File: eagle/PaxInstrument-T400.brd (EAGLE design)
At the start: 99.1 x 53.3 mm, 137 parts, among them IC1 MCP3424, IC3 SN74LVC1G74DCT, J1 MICRO-SDCARD-CONNECTOR-330006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, Q1 DMP2035U-7, Q2 DMP2035U-7, Q3 DMN2075U-7, Q4 DMN2075U-7, Q5 DMP2035U-7, U1 MCP9800, U2 APX809, U3 MCP73831, U4 MIC5219-3.3V, X1 FH12-12S-1S, Y1 RESONATORSMD

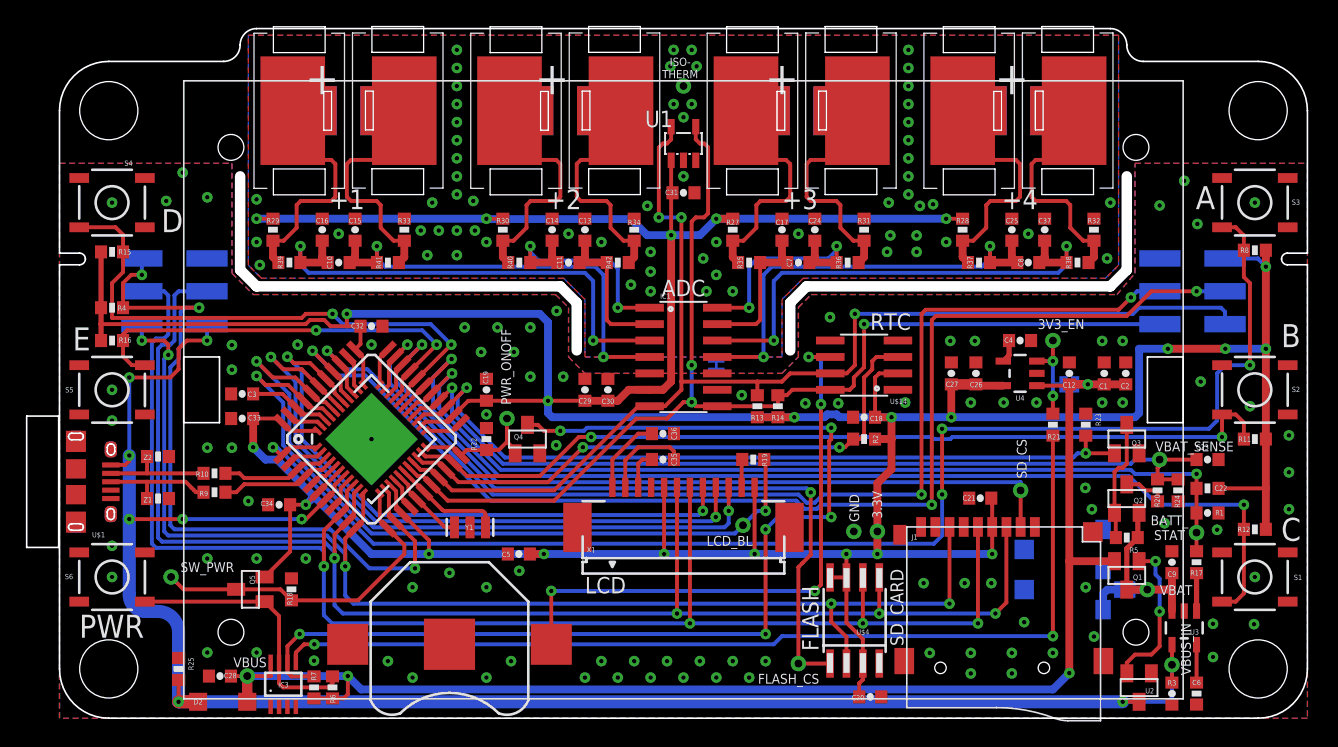
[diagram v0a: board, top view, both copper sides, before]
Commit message: Remove a lot and replace atmega with stm32f103
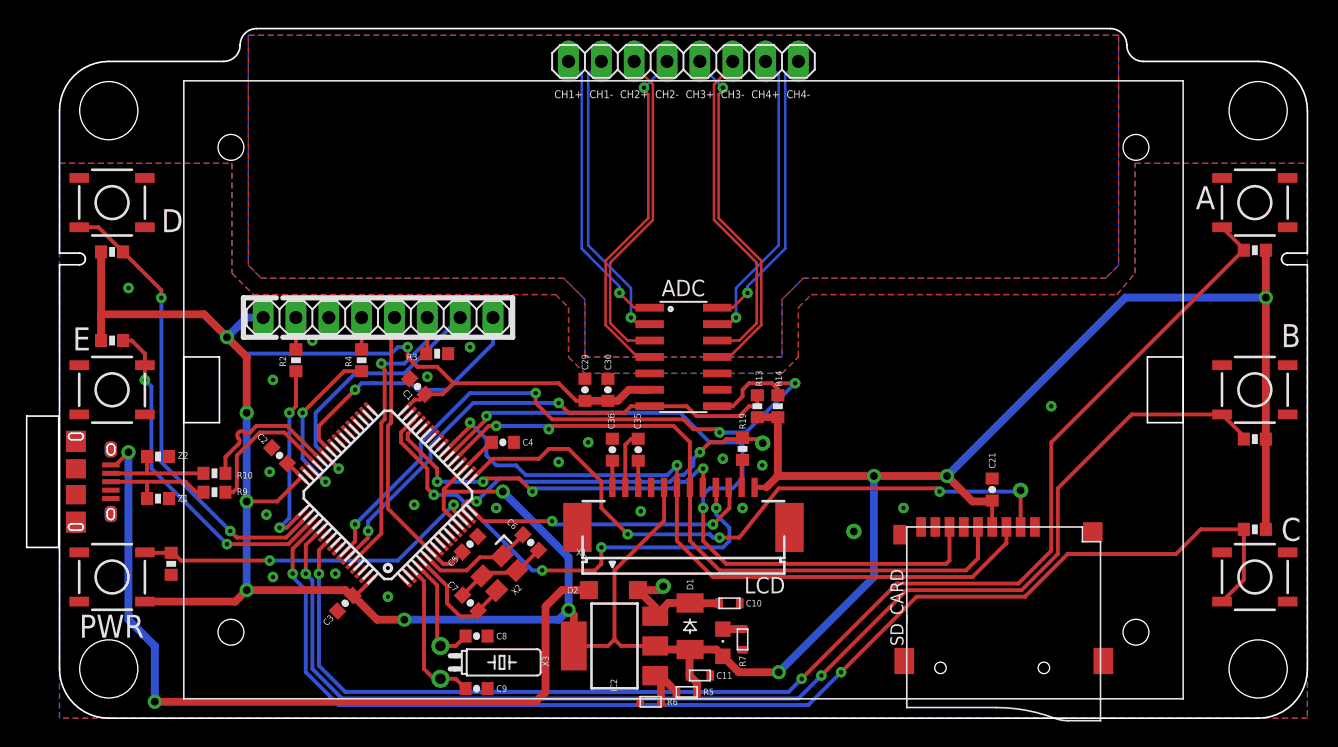
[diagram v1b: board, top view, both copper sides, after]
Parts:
- removed BAT1: (no value), SparkFun-Electromechanical:BATTCON_12MM
- removed C12, C22, C26: 10uF, PaxInstrument-T400:SPARKFUN-CAPACITORS_0603-CAP
- removed C13, C14, C15, C16, C17, C18, C20, C24, C25, C27, C28, C31, C32, C33, C34, C37: 0.1uF, PaxInstrument-T400:SPARKFUN-CAPACITORS_0603-CAP
- removed C19, C23: 1uF, PaxInstrument-T400:SPARKFUN-CAPACITORS_0603-CAP
- removed GND: SPARKFUN-DIGITALIC_QFN_ATMEGA32U4, PaxInstrument-T400:SPARKFUN-DIGITALIC_SPARKFUN-DIGITALIC_QFN-44
- removed IC3: SN74LVC1G74DCT, PaxInstrument-T400:SSOP8
- removed ICSP, ICSP1: ICSP, PaxInstrument-T400:SPARKFUN-CONNECTORS_2X3_SMT_POSTS_PAXINSTRUMENT
- removed JP1: ON, SparkFun-Passives:SJ_2S-NO
- removed Q1, Q2, Q5: DMP2035U-7, PaxInstrument-T400:SOT23
- removed Q3, Q4: DMN2075U-7, PaxInstrument-T400:SOT23
- removed R17: 2k, PaxInstrument-T400:SPARKFUN-RESISTORS_0603-RES
- removed R18, R21, R22, R23: 10k, PaxInstrument-T400:SPARKFUN-RESISTORS_0603-RES
- removed R20: 18.7K, PaxInstrument-T400:SPARKFUN-RESISTORS_0603-RES
- removed R24: 34K, PaxInstrument-T400:SPARKFUN-RESISTORS_0603-RES
- removed R25: 4.7k, PaxInstrument-T400:SPARKFUN-RESISTORS_0603-RES
- removed R27, R28, R29, R30, R31, R32, R33, R34: 1M, PaxInstrument-T400:SPARKFUN-RESISTORS_0603-RES
- removed R35, R36, R37, R38, R39, R40, R41, R42: 499R, PaxInstrument-T400:SPARKFUN-RESISTORS_0603-RES
- removed SJ1, SJ2: JUMPER-PAD-2-NC_BY_TRACE, SparkFun-Passives:PAD-JUMPER-2-NC_BY_TRACE_YES_SILK
- removed TP1: PWR_ONOFF, PaxInstrument-T400:TP_15TH
- removed TP11: VBUS_IN, PaxInstrument-T400:TP_15TH
- removed TP13: 3.3V, PaxInstrument-T400:TP_15TH
- removed TP14: VBAT, PaxInstrument-T400:TP_15TH
- removed TP2: 3V3_EN, PaxInstrument-T400:TP_15TH
- removed TP3: BATT_STAT, PaxInstrument-T400:TP_15TH
- removed TP4: VBAT_SENSE, PaxInstrument-T400:TP_15TH
- removed TP6: FLASH_CS, PaxInstrument-T400:TP_15TH
- removed TP8: ISOTHERMAL, PaxInstrument-T400:TP_15TH
- removed TP9: SW_PWR, PaxInstrument-T400:TP_15TH
- removed U$14: DS3231M, charlespax:SOIC8
- removed U$15, U$16, U$17, U$18, U$19, U$7, U$8, U$9: TC-MINI-SINGLE, PaxInstruments-Connectors:TC-CLIP-SINGLE
- removed U$2: BL-5C-CONNECTOR, charlespax:BL-5C-CONNECTOR
- removed U$3: SPARKFUN-DIGITALIC_ATMEGA32U4TQFP, PaxInstrument-T400:SPARKFUN-DIGITALIC_SPARKFUN-DIGITALIC_TQFP44
- removed U$4: W25Q80DV, PaxInstrument-T400:CHARLESPAX_SOIC8M
- removed U2: APX809, PaxInstrument-T400:SOT23
- removed U3: MCP73831, SparkFun-PowerIC:SOT23-5
- removed U4: MIC5219-3.3V, SparkFun:SOT23-5
- removed Y1: RESONATORSMD, SparkFun:RESONATOR-SMD
- added D1: 1N4148W, diode:SOD-123_MINI-SMA
- added IC2: LM317AEMP, v-reg:SOT223
- added J3, J4: (no value), pinhead:1X08
- added LD1: (no value), adafruit:CHIPLED_0805
- added X2: 16MHz, crystals:FA-238
- added X3: (no value), crystal:TC26H
- C1: value 4.7uF -> 0.1uF
- C10, C11: value 1uF -> 10uF; device PaxInstrument-T400:SPARKFUN-CAPACITORS_0603-CAP -> ell-i:0603
- C4: value 470pF -> 0.1uF
- C6: value 0.1uF -> 18pF
- C7: value 1uF -> 18pF
- C8: value 1uF -> 8pF
- C9: value 4.7uF -> 8pF
- R2, R4: value 10k -> 100
- R3: value 2.32k (1%) -> 10k
- R5: value 10k -> 220R; device PaxInstrument-T400:SPARKFUN-RESISTORS_0603-RES -> ell-i:0603
- R6, R7: value 10k -> 360R; device PaxInstrument-T400:SPARKFUN-RESISTORS_0603-RES -> ell-i:0603
- U1: value MCP9800 -> STM32F10XRXT6; device newparts_2010:SOT23-5L -> stm32:TQFP64
- moved R1 80.4 mm to (8.64, 11.9), turned to 270 degrees
- moved C2 65.8 mm to (17.0, 20.3), turned to 135 degrees
- moved R3 64.4 mm to (29.2, 28.2), turned to 180 degrees
- moved C9 54.7 mm to (32.3, 2.29), turned to 0 degrees
- moved C1 53.1 mm to (27.7, 25.7), turned to 135 degrees
- moved C8 51.5 mm to (32.3, 6.35)
- moved C6 51.0 mm to (36.4, 13.6), turned to 315 degrees
- moved R2 44.4 mm to (18.3, 27.7), turned to 90 degrees
- moved C4 40.8 mm to (34.3, 21.3)
- moved C10 40.1 mm to (51.8, 8.89)
- moved C7 36.6 mm to (31.8, 8.92), turned to 135 degrees
- moved R5 36.1 mm to (48.5, 2.03)
- moved U1 35.5 mm to (25.4, 17.3), turned to 135 degrees
- moved C11 33.5 mm to (49.5, 3.30)
- moved R7 33.4 mm to (52.8, 6.10), turned to 270 degrees
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- renumbered U$1 to J2
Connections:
- removed net 3V3EN: JP1.2, R21.2, TP2.P$1, U4.3
- removed net BATT_STAT: C22.1, GND.27, R1.2, R17.1, TP3.P$1, U$3.27
- removed net DATA1: GND.37, ICSP1.4, U$3.37
- removed net DATA2: GND.36, ICSP1.3, U$3.36
- removed net FLASH_CS: GND.32, TP6.P$1, U$3.32, U$4.1
- removed net ISOTHERMAL: C13.2, C14.2, C15.2, C16.2, C17.1, C24.1, C25.1, C31.2, C37.1, R31.1, R32.1, R33.1, R34.1, SJ2.2, TP8.P$1, U1.2
- removed net N$11: R27.1, R35.2, U$7.P$1
- removed net N$12: Q1.1, U2.2
- removed net N$15: C3.1, GND.42, U$3.42
- removed net N$20: Q2.3, R20.2
- removed net N$26: Q2.1, Q3.3, R5.2
- removed net N$28: IC3.5, R21.1
- removed net N$34: R32.2, R38.1, U$15.P$1
- removed net N$35: R28.1, R37.2, U$9.P$1
- removed net N$40: R30.1, R40.2, U$18.P$1
- removed net PWR_ONOFF: GND.22, Q4.1, R22.1, TP1.P$1, U$3.22
- removed net RESET: GND.13, ICSP.5, R4.1, U$3.13
- removed net RTC_BATT: BAT1.PWR@1, U$14.6
- removed net RTC_INT: GND.20, R2.2, U$14.3, U$3.20
- removed net RXLED: GND.8, U$3.8
- removed net TC1+: C10.1, C16.1, IC1.3, R39.1
- removed net TC1-: C10.2, C15.1, IC1.4, R41.2
- removed net TC2+: C11.1, C14.1, IC1.1, R40.1
- removed net TC2-: C11.2, C13.1, IC1.2, R42.2
- removed net TC3+: C17.2, C7.1, IC1.13, R35.1
- removed net TC3-: C24.2, C7.2, IC1.14, R36.2
- removed net TC4+: C25.2, C8.1, IC1.11, R37.1
- removed net TC4-: C37.2, C8.2, IC1.12, R38.2
- removed net VBAT_EN: GND.25, Q3.1, R23.2, U$3.25
- removed net VBAT_SENSE: C23.1, GND.26, R20.1, R24.1, TP4.P$1, U$3.26
- removed net XTAL1: GND.17, U$3.17, Y1.1
- removed net XTAL2: GND.16, U$3.16, Y1.3
- new net ADC_CH1_N: IC1.2, J3.7
- new net ADC_CH1_P: IC1.1, J3.8
- new net ADC_CH2_N: IC1.4, J3.5
- new net ADC_CH2_P: IC1.3, J3.6
- new net ADC_CH3_N: IC1.12, J3.3
- new net ADC_CH3_P: IC1.11, J3.4
- new net ADC_CH4_N: IC1.14, J3.1
- new net ADC_CH4_P: IC1.13, J3.2
- new net BOOT0: J4.6, R3.2, U1.60
- new net NRST: C5.1, J4.5, U1.7
- new net SWCLK: R2.1, U1.49
- new net SWDIO: R4.1, U1.46
- new net UART_RX: J4.7, U1.43
- new net UART_TX: J4.8, U1.42
- net 3.3V: now also C1.1, C11.1, C2.1, C3.1, C4.1, D1.A, IC2.2, IC2.4, J4.1, LD1.A, R5.1, S6.1, U1.13, U1.19, U1.32, U1.48, U1.64; no longer C18.1, C19.1, C20.2, C26.1, C27.1, C31.1, C32.1, C33.1, C34.1, C5.1, GND.14, GND.24, GND.34, GND.44, GND.6, ICSP1.6, Q5.2, R1.1, R2.1, R27.2, R28.2, R29.2, R30.2, R4.2, TP13.P$1, U$14.2, U$3.14, U$3.24, U$3.34, U$3.44, U$3.6, U$4.3, U$4.7, U$4.8, U1.1, U4.5
- net D+: now also R10.2, U1.44; no longer GND.4, R9.2, U$3.4
- net D-: now also R9.2, U1.45; no longer GND.3, R10.2, U$3.3
- net GND: now also C10.2, C11.2, C7.2, C8.2, J4.3, R1.2, R3.1, R6.2, R7.2, U1.12, U1.18, U1.31, U1.47, U1.63, X2.2, X2.4; no longer BAT1.GND, C12.2, C18.2, C19.2, C2.2, C20.1, C22.2, C23.2, C26.2, C27.2, C28.2, C3.2, C32.2, C33.2, C34.2, C4.2, GND.15, GND.23, GND.33, GND.35, GND.43, GND.5, GND.P$1, IC3.1, IC3.2, IC3.4, ICSP.6, ICSP1.5, Q3.2, Q4.2, R18.2, R22.2, R23.1, R24.2, R25.1, R3.2, S6.3, SJ2.1, U$14.5, U$2.P$3, U$2.P$4, U$2.P$5, U$3.15, U$3.23, U$3.33, U$3.35, U$3.43, U$3.5, U$4.4, U2.1, U3.2, U4.2, Y1.2
- net LCD_A0: now also U1.29; no longer GND.38, U$3.38
- net LCD_BL: now also U1.15; no longer GND.41, U$3.41
- net LCD_CS: now also U1.16; no longer GND.40, U$3.40
- net LCD_RST: now also U1.30; no longer GND.39, U$3.39
- net MISO: now also U1.22; no longer GND.11, ICSP.1, U$3.11, U$4.2
- net MOSI: now also U1.23; no longer GND.10, ICSP.4, U$3.10, U$4.5
- net N$1: now also C7.1, U1.5, X2.3; no longer C4.1, U4.4
- net N$10: now also LD1.C, R7.1; no longer SJ1.2, U$2.P$1
- net N$13: now also C3.2; no longer R29.1, R39.2, U$16.P$1
- net N$14: now also C4.2; no longer R33.2, R41.1, U$17.P$1
- net N$16: now also C8.1, U1.4, X3.1; no longer R34.2, R42.1, U$19.P$1
- net N$17: now also C9.1, U1.3, X3.2; no longer GND.2, U$3.2
- net N$2: now also C2.2; no longer R17.2, U3.1
- net N$25: now also J4.2, R2.2; no longer IC3.7, Q5.1, R6.2, S6.1
- net N$27: now also J4.4, R4.2; no longer IC3.6, Q4.3, R7.2
- net N$5: now also C6.1, U1.6, X2.1; no longer R31.2, R36.1, U$8.P$1
- net N$7: now also IC2.1, R5.2, R6.1; no longer R3.1, U3.5
- net SCK: now also U1.21; no longer GND.9, ICSP.3, U$3.9, U$4.6
- net SCL: now also U1.58; no longer GND.18, ICSP1.1, U$14.8, U$3.18, U1.4
- net SDA: now also U1.59; no longer GND.19, ICSP1.2, U$14.7, U$3.19, U1.5
- net SD_CS: now also U1.17; no longer GND.31, U$3.31
- net SW_A: now also U1.55; no longer GND.1, U$3.1
- net SW_B: now also U1.53; no longer GND.21, U$3.21
- net SW_C: now also U1.52; no longer GND.28, U$3.28
- net SW_D: now also U1.50; no longer GND.29, U$3.29
- net SW_E: now also U1.51; no longer GND.30, U$3.30
- net SW_PWR: now also R1.1, S6.3, U1.14; no longer GND.12, Q5.3, R18.1, TP9.P$1, U$3.12
- net VBAT: now also U1.1; no longer C9.1, Q1.3, Q2.2, R5.1, SJ1.1, TP14.P$1, U3.3
- net VBUS: now also C10.1, D1.C, IC2.3; no longer C1.1, C12.1, C2.1, C28.1, IC3.8, JP1.1, Q1.2, R6.1, R7.1, U4.1
- net VBUS_IN: no longer C6.1, GND.7, ICSP.2, R25.2, TP11.P$1, U$3.7, U2.3, U3.4
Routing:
- net 3.3V: track 387.4 -> 284.0 mm, vias 23 -> 12
- net VBUS: track 110.0 -> 10.0 mm, vias 3 -> 0
- net DATA1: track 95.9 -> 0.00 mm, vias 3 -> 0
- net DATA2: track 88.5 -> 0.00 mm, vias 3 -> 0
- net N$27: track 86.0 -> 2.45 mm, vias 6 -> 0
- net VBUS_IN: track 143.9 -> 62.9 mm, vias 8 -> 2
- net N$28: track 75.3 -> 0.00 mm, vias 2 -> 0
- net BATT_STAT: track 74.5 -> 0.00 mm, vias 2 -> 0
- net VBAT_SENSE: track 68.5 -> 0.00 mm, vias 1 -> 0
- net SCK: track 120.5 -> 53.5 mm, vias 4 -> 2
- net MOSI: track 117.7 -> 56.4 mm, vias 4 -> 2
- net VBAT_EN: track 60.8 -> 0.00 mm, vias 2 -> 0
- net FLASH_CS: track 59.9 -> 0.00 mm, vias 2 -> 0
- net RESET: track 56.6 -> 0.00 mm, vias 3 -> 0
- net SDA: track 96.6 -> 40.0 mm, vias 3 -> 2
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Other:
- outline, holes or cut-outs redrawn
- board text added: "CH1+"
- board text added: "CH1-"
- board text added: "CH2+"
- board text added: "CH2-"
- board text added: "CH3+"
- board text added: "CH3-"
- board text added: "CH4+"
- board text added: "CH4-"
- board text added: "I2C Addresses: - ADC MCP3424 0x69"
- board text added: "TXXX v0.0.1"
- board text added: "paxinstruments.com/products/unreleased"
- board text removed: "+"
- board text removed: "+1"
- board text removed: "+2"
- board text removed: "+3"
- board text removed: "+4"
- board text removed: "12c Addresses: - ADC MCP3424 0x69 - Temp MCP9800 0x48 - RTC DS3231 0x68"
- board text removed: "3.3V"
- board text removed: "3V3_EN"
- board text removed: "ALWAYS ON JUMPER"
- board text removed: "Arduino pin map D0 RTC_INT D1 SW_B D2 SDA D3 SCL D4 VBAT_EN D5 SD_CS D6 BATT_STAT D7 SW_A D8 SW_C D9 SW_D D10 SW_E D11 SW_PWR"
- board text removed: "BATT_ STAT"
- board text removed: "BATT_STAT"
- board text removed: "D12 VBAT_SENSE D13 FLASH_CS D14 MISO D15 SCK D16 MOSI D17 RXLED A0 DATA2 A1 DATA1 A2 LCD_A0 A3 LCD_RST A4 LCD_CS A5 LCD_BL"
- board text removed: "DATA1"
- board text removed: "DATA2"
- board text removed: "FLASH"
- board text removed: "FLASH_CS"
- board text removed: "GND"
- board text removed: "ISO- THERM"
- board text removed: "LCD_BL"
- board text removed: "MISO"
- board text removed: "MOSI"
- board text removed: "PWR_ONOFF"
- board text removed: "RST"
- board text removed: "RTC"
- board text removed: "SCK"
- board text removed: "SCL"
- board text removed: "SDA"
- board text removed: "SD_CS"
- board text removed: "SW_PWR"
- board text removed: "T400 v0.14"
- board text removed: "VBAT"
- board text removed: "VBAT_SENSE"
- board text removed: "VBUS"
- board text removed: "VBUS_IN"
- board text removed: "VCC"
- board text removed: "paxinstruments.com/products/sku927"

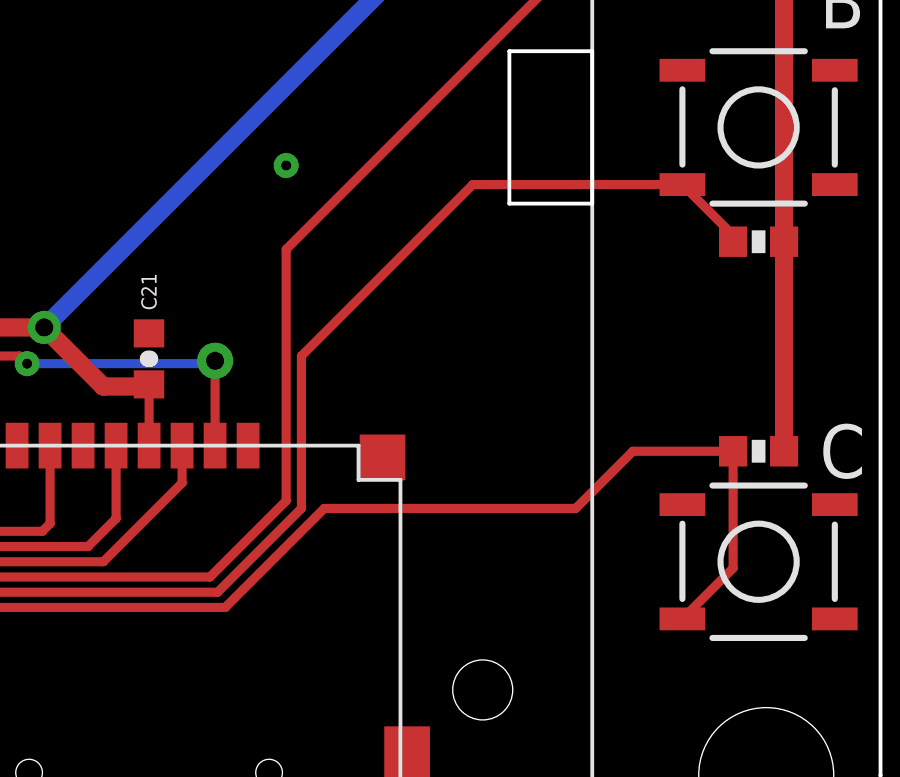
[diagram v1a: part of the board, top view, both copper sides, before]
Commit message: Moved a trace that was inside the LCD cutout
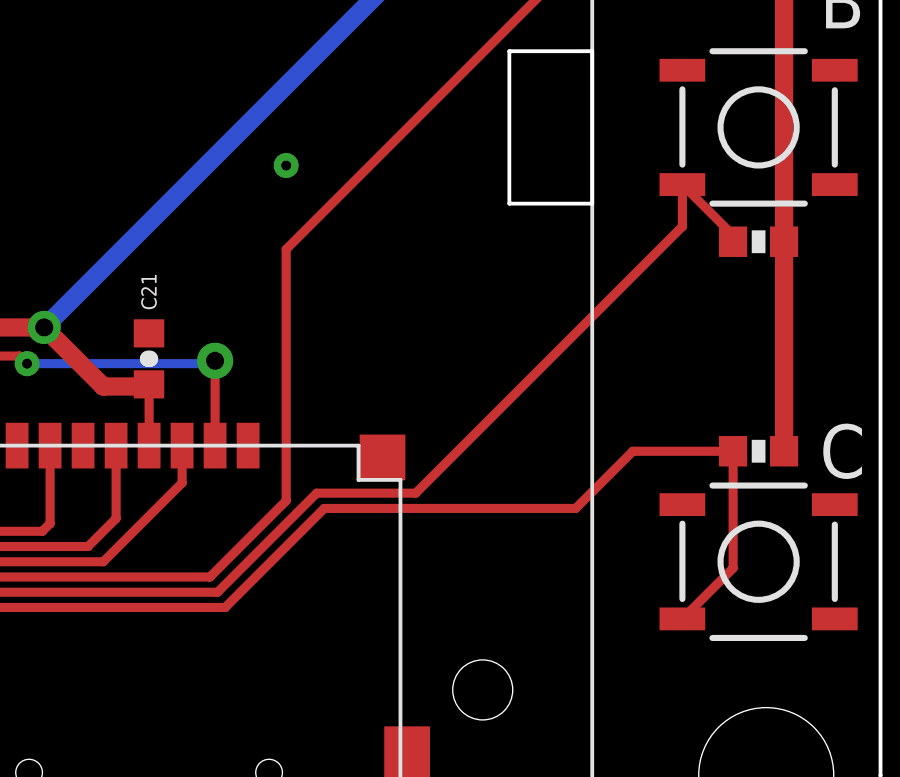
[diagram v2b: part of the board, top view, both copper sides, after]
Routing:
- net SW_B: track 97.3 -> 95.2 mm
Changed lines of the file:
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@@
 <layer number="44" name="Drills" color="7" fill="1" visible="no" active="yes"/>
 <layer number="45" name="Holes" color="7" fill="1" visible="no" active="yes"/>
-<layer number="46" name="Milling" color="3" fill="1" visible="no" active="yes"/>
+<layer number="46" name="Milling" color="3" fill="1" visible="yes" active="yes"/>
 <layer number="47" name="Measures" color="7" fill="1" visible="no" active="yes"/>
 <layer number="48" name="Document" color="7" fill="1" visible="no" active="yes"/>
@@
 <wire x1="91.606" y1="21.805" x2="89.916" y2="23.495" width="0.3048" layer="1"/>
 <contactref element="U1" pad="53"/>
-<wire x1="89.916" y1="23.495" x2="82.931" y2="23.495" width="0.3048" layer="1"/>
-<wire x1="82.931" y1="23.495" x2="77.216" y2="17.78" width="0.3048" layer="1"/>
-<wire x1="77.216" y1="17.78" x2="77.216" y2="12.7" width="0.3048" layer="1"/>
-<wire x1="77.216" y1="12.7" x2="74.422" y2="9.906" width="0.3048" layer="1"/>
+<wire x1="77.724" y1="13.208" x2="74.422" y2="9.906" width="0.3048" layer="1"/>
 <wire x1="74.422" y1="9.906" x2="65.532" y2="9.906" width="0.3048" layer="1"/>
 <wire x1="65.532" y1="9.906" x2="58.928" y2="3.302" width="0.3048" layer="1"/>
@@
 <wire x1="19.05" y1="11.176" x2="19.05" y2="13.396875" width="0.3048" layer="1"/>
 <wire x1="19.05" y1="13.396875" x2="20.132053125" y2="14.478928125" width="0.3048" layer="1"/>
+<wire x1="77.724" y1="13.208" x2="81.026" y2="13.208" width="0.3048" layer="1"/>
+<wire x1="81.026" y1="13.208" x2="89.916" y2="22.098" width="0.3048" layer="1"/>
+<wire x1="89.916" y1="22.098" x2="89.916" y2="23.495" width="0.3048" layer="1"/>
 </signal>
 <signal name="SW_C">
